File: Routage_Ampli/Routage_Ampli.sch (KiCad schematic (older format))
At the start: 52 parts, among them Q1 2N2907, Q10 TIP32, Q11 BD138, Q12 TIP31, Q13 2N2222, Q2 2N2907, Q3 2N2907, Q4 2N2222, Q5 2N2222, Q6 2N2907, Q7 2N2907, Q8 BD139, Q9 BD139

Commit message: Début Placement + Routage
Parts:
- C1, C3: value 47u -> 47µ; footprint (none) -> CmpAmpliAudio:CP_Radial_D8.0mm_P5.00mm
- C10, C8: value 470u -> 470µ; footprint (none) -> CmpAmpliAudio:CP_Radial_D12.5mm_P5.00mm
- C11, C2, C5, C7, C9: footprint (none) -> CmpAmpliAudio:C_Rect_L7.2mm_W3.5mm_P5.00mm_FKS2_FKP2_MKS2_MKP2
- C4, C6: value 10u -> 10µ; footprint (none) -> CmpAmpliAudio:CP_Radial_D8.0mm_P5.00mm
- D1, D2: footprint Diode_THT:D_DO-35_SOD27_P7.62mm_Horizontal -> CmpAmpliAudio:D_DO-35_SOD27_P10.16mm_Horizontal
- Dz1: footprint (none) -> CmpAmpliAudio:D_DO-35_SOD27_P10.16mm_Horizontal
- HS1, HS2: footprint (none) -> CmpAmpliAudio:Heatsink_Fischer_SK104-STC-STIC_35x13mm_2xDrill2.5mm
- J1: renamed from J?; footprint (none) -> CmpAmpliAudio:PhoenixContact_MSTBVA_2,5_3-G-5,08_1x03_P5.08mm_Vertical
- J2: renamed from J?; footprint (none) -> CmpAmpliAudio:PhoenixContact_MSTBVA_2,5_2-G-5,08_1x02_P5.08mm_Vertical
- Q1, Q13, Q2, Q3, Q4, Q5, Q6, Q7: footprint (none) -> CmpAmpliAudio:TO-18-3
- Q10, Q12: footprint (none) -> CmpAmpliAudio:TO-220-3_Vertical
- Q11, Q8, Q9: footprint (none) -> CmpAmpliAudio:TO-126-3_Vertical
- R1, R13, R14, R15, R16, R2, R3, R4, R5, R6, R7, R8, R9: footprint (none) -> CmpAmpliAudio:R_Axial_DIN0207_L6.3mm_D2.5mm_P10.16mm_Horizontal
- R10, R17: renamed from R?; footprint (none) -> CmpAmpliAudio:R_Axial_DIN0207_L6.3mm_D2.5mm_P10.16mm_Horizontal
- R11, R12: footprint (none) -> CmpAmpliAudio:R_Axial_DIN0516_L15.5mm_D5.0mm_P20.32mm_Horizontal
- RV1, RV2: footprint (none) -> CmpAmpliAudio:Potentiometer_Bourns_3296W_Vertical
- U1: renamed from U??; footprint (none) -> CmpAmpliAudio:Jack_35RAPC2AV
- U2: renamed from U??; footprint (none) -> Routage_Ampli:Relay_CT
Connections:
- net at Q6.3 (C), Q8.2 (C), Q9.3 (B): now also RV1.1
- no-connect marks 0 -> 1

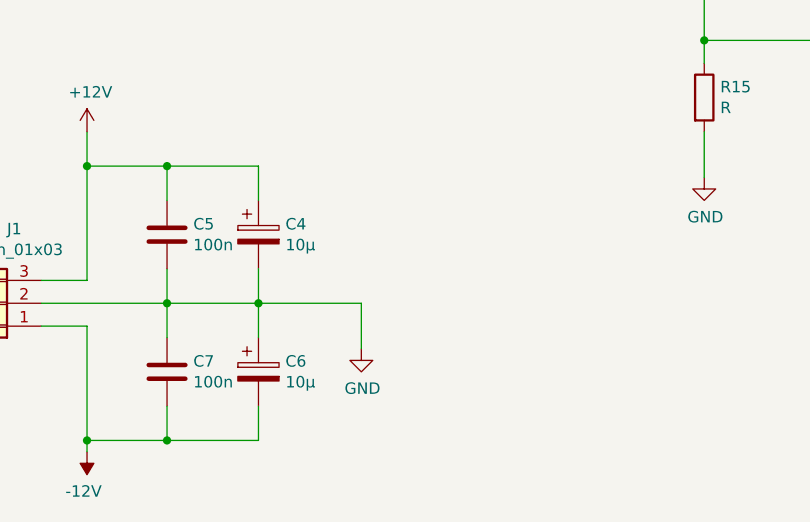
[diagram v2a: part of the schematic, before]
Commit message: Derniers détails
Ajout de derniers détails : Texte en bottom, diodes de protection, mise à jour de la lib
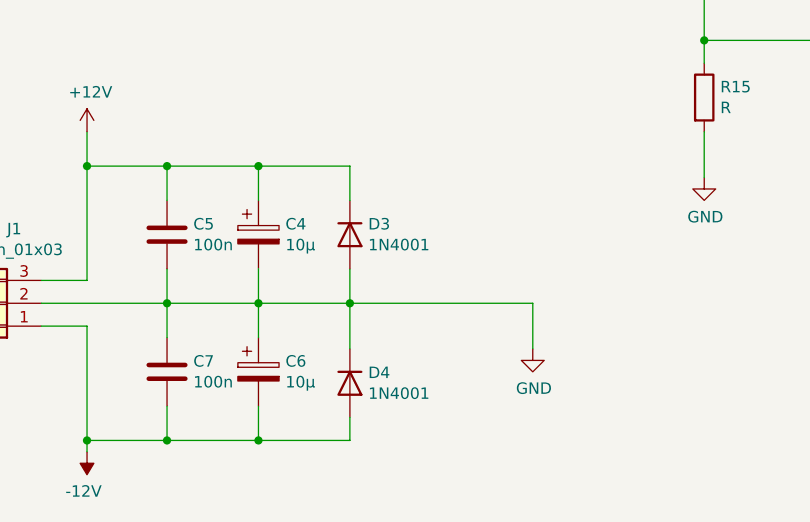
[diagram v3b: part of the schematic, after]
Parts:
- added D3, D4: 1N4001, CmpAmpliAudio:D_DO-35_SOD27_P10.16mm_Horizontal, symbol Device:D
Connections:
- net +12V: now also D3.1 (K)
- net -12V: now also D4.2 (A)
- net GND: now also D3.2 (A), D4.1 (K)
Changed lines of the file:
@@
 L power:GND #PWR05
 U 1 1 60522EC6
-P 2650 6800
-F 0 "#PWR05" H 2650 6550 50  0001 C CNN
-F 1 "GND" H 2655 6627 50  0000 C CNN
-F 2 "" H 2650 6800 50  0001 C CNN
-F 3 "" H 2650 6800 50  0001 C CNN
-	1    2650 6800
-	1    0    0    -1
-$EndComp
-Wire Wire Line
-	2200 6600 2650 6600
-Wire Wire Line
-	2650 6600 2650 6800
+P 3400 6800
+F 0 "#PWR05" H 3400 6550 50  0001 C CNN
+F 1 "GND" H 3405 6627 50  0000 C CNN
+F 2 "" H 3400 6800 50  0001 C CNN
+F 3 "" H 3400 6800 50  0001 C CNN
+	1    3400 6800
+	1    0    0    -1
+$EndComp
+Wire Wire Line
+	3400 6600 3400 6800
 $Comp
 L Connector_Generic:Conn_01x03 J1
@@
 	1    0    0    1
 $EndComp
+Wire Wire Line
+	2600 6150 2600 6000
+Wire Wire Line
+	2600 6000 2200 6000
+Connection ~ 2200 6000
+Wire Wire Line
+	2600 6600 2600 6450
+Wire Wire Line
+	2600 6600 2200 6600
+Connection ~ 2600 6600
+Wire Wire Line
+	2600 6800 2600 6600
+Wire Wire Line
+	2600 7100 2600 7200
+Wire Wire Line
+	2600 7200 2200 7200
+Connection ~ 2200 7200
+Wire Wire Line
+	2600 6600 3400 6600
+$Comp
+L Device:D D3
+U 1 1 607DBEB2
+P 2600 6300
+F 0 "D3" V 2554 6380 50  0000 L CNN
+F 1 "1N4001" V 2645 6380 50  0000 L CNN
+F 2 "CmpAmpliAudio:D_DO-35_SOD27_P10.16mm_Horizontal" H 2600 6300 50  0001 C CNN
+F 3 "~" H 2600 6300 50  0001 C CNN
+	1    2600 6300
+	0    1    1    0
+$EndComp
+$Comp
+L Device:D D4
+U 1 1 607DD0B1
+P 2600 6950
+F 0 "D4" V 2554 7030 50  0000 L CNN
+F 1 "1N4001" V 2645 7030 50  0000 L CNN
+F 2 "CmpAmpliAudio:D_DO-35_SOD27_P10.16mm_Horizontal" H 2600 6950 50  0001 C CNN
+F 3 "~" H 2600 6950 50  0001 C CNN
+	1    2600 6950
+	0    1    1    0
+$EndComp
 $EndSCHEMATC
